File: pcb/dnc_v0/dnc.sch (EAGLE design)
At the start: 59 parts, among them IC1 74HC595D, IC2 74HC595D, Q1 200mA/50V, Q2 TSM2306CX, Q3 TSM2306CX, Q4 TSM2306CX, Q6 200mA/50V

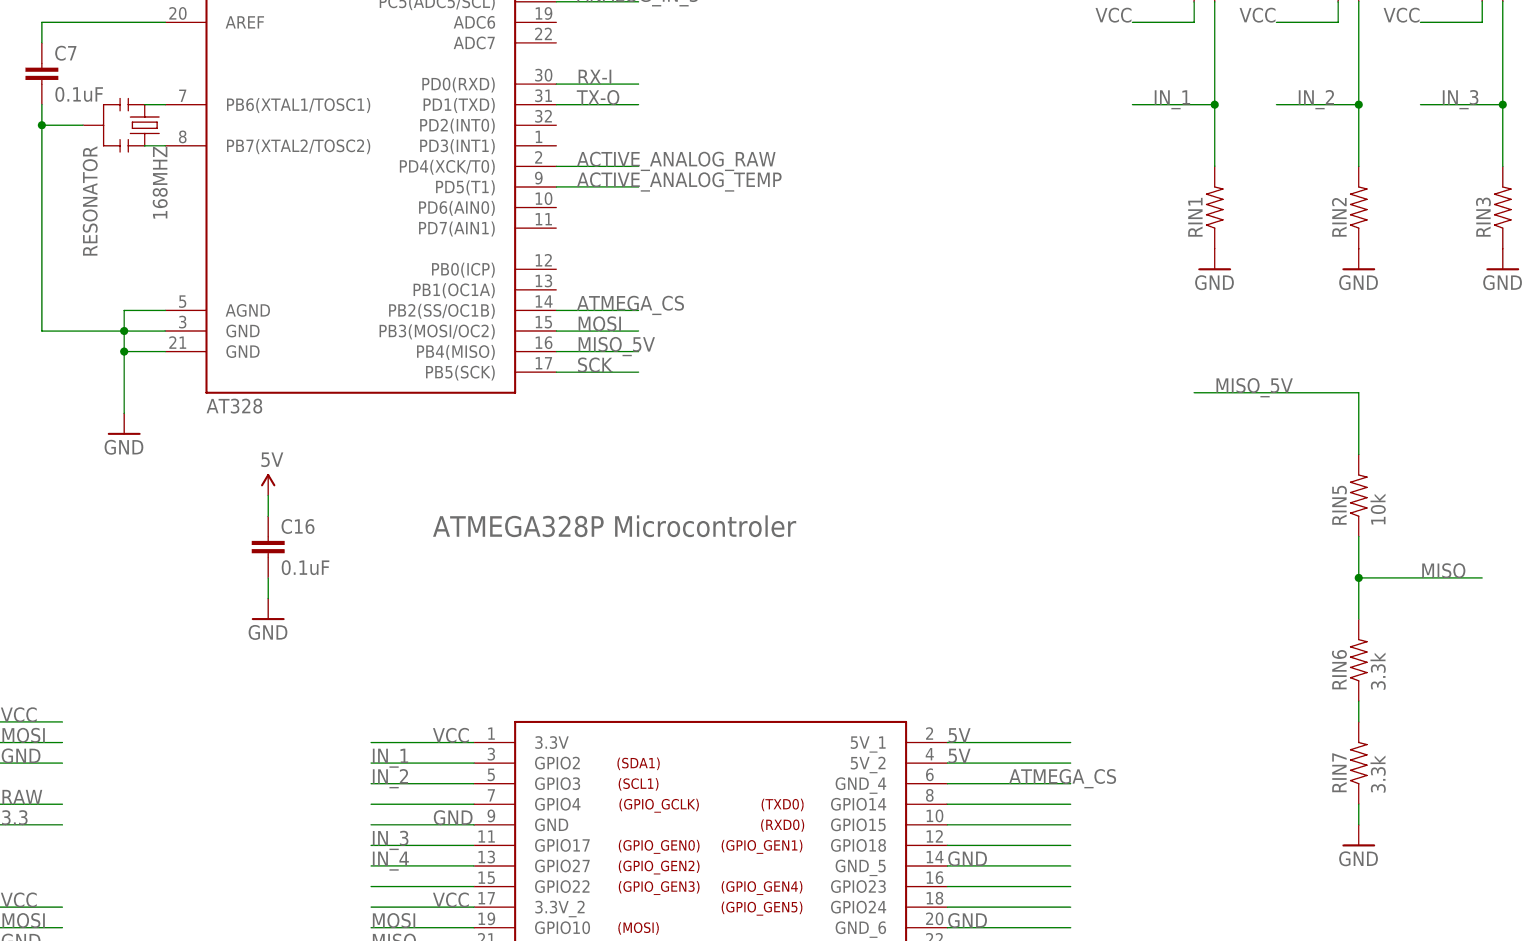
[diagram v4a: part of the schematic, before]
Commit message: Reorganize ATmega to work with 5V with Zener diode
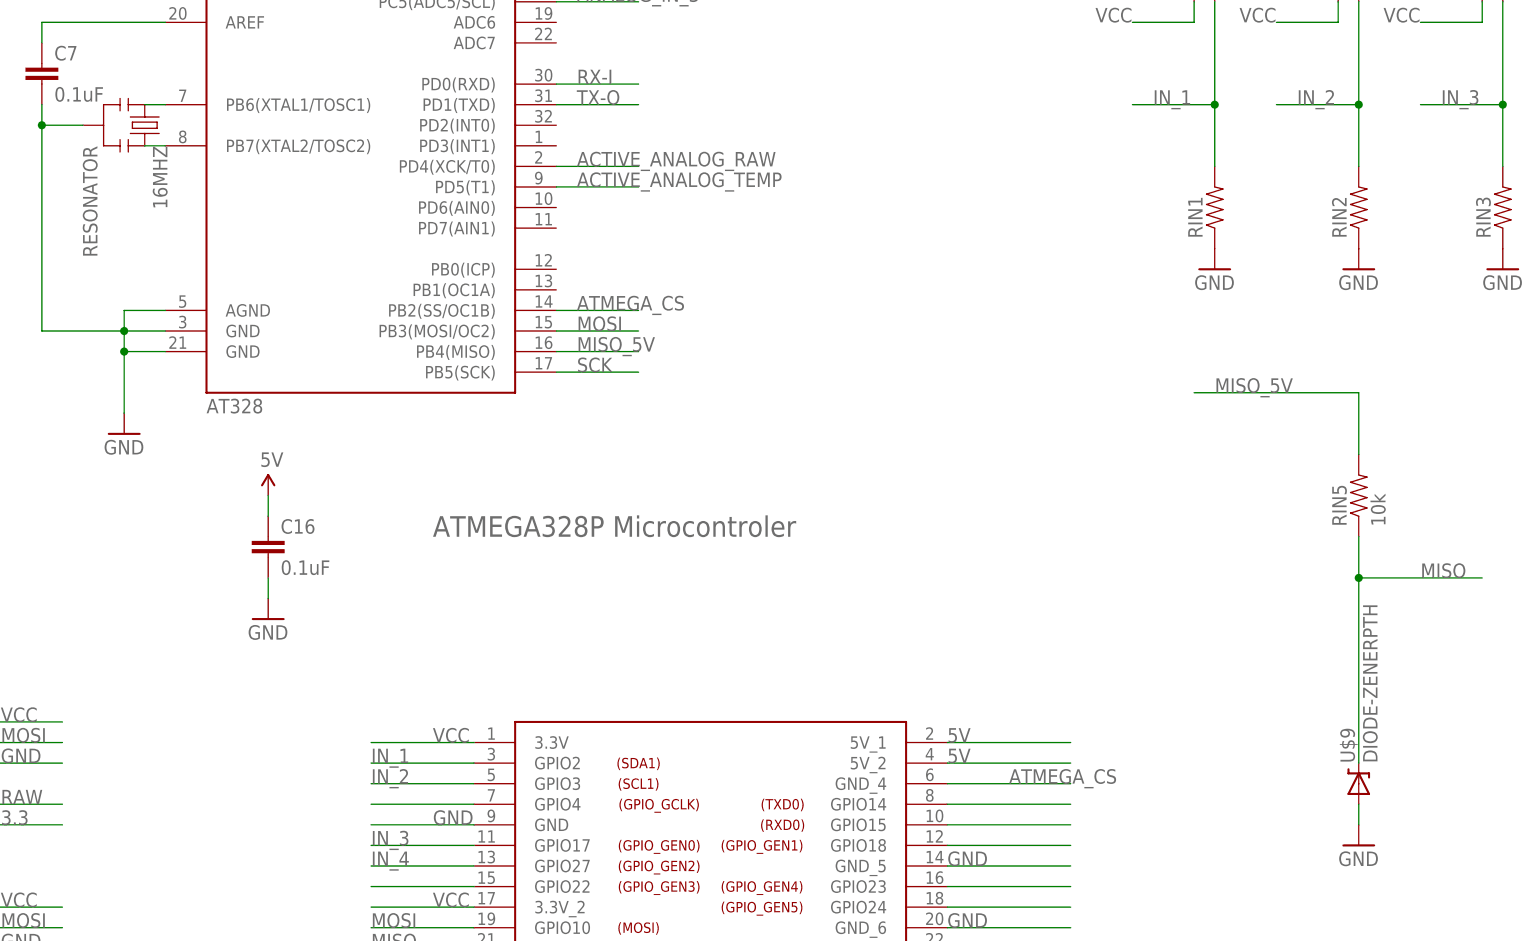
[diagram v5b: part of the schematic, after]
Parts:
- removed RIN6, RIN7: 3.3k, SparkFun-Passives:RESISTOR0603-RES
- added U$9: DIODE-ZENERPTH, SparkFun-DiscreteSemi:DIODE-ZENERPTH
- renumbered 168MHZ to 16MHZ
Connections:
- removed net N$6: RIN6.1, RIN7.2
- net GND: now also U$9.A; no longer RIN7.1
- net MISO: now also U$9.C; no longer RIN6.2
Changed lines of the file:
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@@
 <part name="GND36" library="SparkFun" deviceset="GND" device=""/>
 <part name="AT328" library="SparkFun" deviceset="ATMEGA168" device=""/>
-<part name="168MHZ" library="pierre_vv" deviceset="RESONATOR" device=""/>
+<part name="16MHZ" library="pierre_vv" deviceset="RESONATOR" device=""/>
 <part name="U$17" library="SparkFun" deviceset="5V" device="" value="5V"/>
 <part name="U$18" library="SparkFun" deviceset="5V" device=""/>
@@
 <part name="JP1" library="SparkFun-Connectors" deviceset="M02" device="5MM" value="M025MM"/>
 <part name="RIN5" library="SparkFun-Passives" deviceset="RESISTOR" device="0603-RES" value="10k"/>
-<part name="RIN6" library="SparkFun-Passives" deviceset="RESISTOR" device="0603-RES" value="3.3k"/>
-<part name="RIN7" library="SparkFun-Passives" deviceset="RESISTOR" device="0603-RES" value="3.3k"/>
 <part name="GND2" library="SparkFun-Aesthetics" deviceset="GND" device=""/>
+<part name="U$9" library="SparkFun-DiscreteSemi" deviceset="DIODE-ZENER" device="PTH"/>
 </parts>
 <sheets>
@@
 <instance part="GND36" gate="1" x="33.02" y="15.24"/>
 <instance part="AT328" gate="G$1" x="43.18" y="78.74"/>
-<instance part="168MHZ" gate="G$1" x="15.24" y="76.2" rot="R270"/>
+<instance part="16MHZ" gate="G$1" x="15.24" y="76.2" rot="R270"/>
 <instance part="U$17" gate="G$1" x="5.08" y="109.22"/>
 <instance part="U$18" gate="G$1" x="-38.1" y="99.06"/>
@@
 <instance part="JP1" gate="G$1" x="-160.02" y="96.52" rot="MR180"/>
 <instance part="RIN5" gate="G$1" x="167.64" y="30.48" rot="R90"/>
-<instance part="RIN6" gate="G$1" x="167.64" y="10.16" rot="R90"/>
-<instance part="RIN7" gate="G$1" x="167.64" y="-2.54" rot="R90"/>
 <instance part="GND2" gate="1" x="167.64" y="-12.7"/>
+<instance part="U$9" gate="G$1" x="167.64" y="-5.08" rot="R90"/>
 </instances>
 <busses>
@@
 <pinref part="AT328" gate="G$1" pin="GND@2"/>
 <pinref part="AT328" gate="G$1" pin="AGND"/>
-<pinref part="168MHZ" gate="G$1" pin="2"/>
+<pinref part="16MHZ" gate="G$1" pin="2"/>
 </segment>
 <segment>
@@
 </segment>
 <segment>
-<pinref part="RIN7" gate="G$1" pin="1"/>
 <pinref part="GND2" gate="1" pin="GND"/>
 <wire x1="167.64" y1="-7.62" x2="167.64" y2="-10.16" width="0.1524" layer="91"/>
+<pinref part="U$9" gate="G$1" pin="A"/>
 </segment>
 </net>
@@
 <segment>
 <pinref part="RIN5" gate="G$1" pin="1"/>
-<pinref part="RIN6" gate="G$1" pin="2"/>
 <wire x1="167.64" y1="25.4" x2="167.64" y2="20.32" width="0.1524" layer="91"/>
-<wire x1="167.64" y1="20.32" x2="167.64" y2="15.24" width="0.1524" layer="91"/>
 <wire x1="167.64" y1="20.32" x2="182.88" y2="20.32" width="0.1524" layer="91"/>
 <junction x="167.64" y="20.32"/>
 <label x="175.26" y="20.32" size="1.778" layer="95"/>
+<pinref part="U$9" gate="G$1" pin="C"/>
+<wire x1="167.64" y1="20.32" x2="167.64" y2="-2.54" width="0.1524" layer="91"/>
 </segment>
 </net>
@@
 <segment>
 <wire x1="17.78" y1="78.74" x2="20.32" y2="78.74" width="0.1524" layer="91"/>
-<pinref part="168MHZ" gate="G$1" pin="1"/>
+<pinref part="16MHZ" gate="G$1" pin="1"/>
 <pinref part="AT328" gate="G$1" pin="PB6(XTAL1/TOSC1)"/>
 </segment>
@@
 <segment>
 <wire x1="17.78" y1="73.66" x2="20.32" y2="73.66" width="0.1524" layer="91"/>
-<pinref part="168MHZ" gate="G$1" pin="3"/>
+<pinref part="16MHZ" gate="G$1" pin="3"/>
 <pinref part="AT328" gate="G$1" pin="PB7(XTAL2/TOSC2)"/>
 </segment>
@@
 </segment>
 </net>
-<net name="N$6" class="0">
-<segment>
-<pinref part="RIN6" gate="G$1" pin="1"/>
-<pinref part="RIN7" gate="G$1" pin="2"/>
-<wire x1="167.64" y1="5.08" x2="167.64" y2="2.54" width="0.1524" layer="91"/>
-</segment>
-</net>

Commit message: Reorganize ATmega to work with 3.3V
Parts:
- removed RIN5: 10k, SparkFun-Passives:RESISTOR0603-RES
- removed U$9: DIODE-ZENERPTH, SparkFun-DiscreteSemi:DIODE-ZENERPTH
- added JP12, JP20, JP21: M02LOCK_LONGPADS, SparkFun-Connectors:M02LOCK_LONGPADS
- added R10, R11, R9: 10k, SparkFun-Passives:RESISTOR0603-RES
- R5, R6, R7: value (none) -> 100k
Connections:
- removed net MISO_5V: RIN5.2
- new net N$1: JP12.1, R9.2
- new net N$13: JP21.1, R11.2
- new net N$6: JP20.1, R10.2
- net 5V: no longer AT328.AVCC, AT328.VCC@1, AT328.VCC@2
- net ACTIVE_OUT_POWER_2: now also AT328.PD3(INT1)
- net ACTIVE_OUT_POWER_3: now also AT328.PD6(AIN0)
- net GND: now also JP12.2, JP20.2, JP21.2, R10.1, R11.1, R9.1; no longer U$9.A
- net MISO: no longer RIN5.1, U$9.C
- net VCC: now also AT328.AVCC, AT328.VCC@1, AT328.VCC@2

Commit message: Reogranise with 3.3, 5 and RAW
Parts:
- removed R10, R11, R9: 10k, SparkFun-Passives:RESISTOR0603-RES
- removed R5, R6, R7: 100k, SparkFun-Passives:RESISTOR0603-RES
- added JP22: (no value), SparkFun:M02PTH3
- added Q5, Q7, Q8: TSM2306CX, SparkFun-DiscreteSemi:MOSFET-NCHANNEL2N7002PW
- added RIN10, RIN5, RIN6, RIN7, RIN8, RIN9: 100k, SparkFun-Passives:RESISTOR0603-RES
- renumbered 16MHZ to 8MHZ
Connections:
- removed net 5V: C16.1, ISP1.2, JP2.2, JP3.2, JP4.2, PROG1.VCC, R26.2, R3.1, U$4.5V_1, U$4.5V_2, U$5.OUT+
- removed net N$1: JP12.1, R9.2
- removed net N$13: JP21.1, R11.2
- removed net N$26: R6.2
- removed net N$27: U$4.GPIO19
- removed net N$28: U$4.GPIO26
- removed net N$29: Q4.S, R7.2
- removed net N$40: U$4.GPIO12
- removed net N$6: JP20.1, R10.2
- new net +3V3: AT328.AVCC, AT328.VCC@1, AT328.VCC@2, C16.1, IC1A.SCL, IC2A.SCL, ISP1.2, JP2.2, JP22.1, JP3.2, JP4.2, JP5.1, JP6.1, JP7.1, JP8.1, PROG1.VCC, R26.2, U$4.3.3V, U$4.3.3V_2
- new net +5V: JP22.2, Q2.D, Q3.D, Q4.D, Q5.D, Q7.D, Q8.D, R3.1, U$4.5V_1, U$4.5V_2, U$5.OUT+
- new net ACTIVE_OUT_1: Q5.G, RIN8.2, U$4.GPIO12
- new net ACTIVE_OUT_2: Q7.G, RIN9.2, U$4.GPIO19
- new net ACTIVE_OUT_3: Q8.G, RIN10.2, U$4.GPIO26
- new net OUT_1: JP12.1, Q5.S
- new net OUT_2: JP20.1, Q7.S
- new net OUT_3: JP21.1, Q8.S
- net ACTIVE_OUT_POWER_1: now also RIN5.2
- net ACTIVE_OUT_POWER_2: now also RIN6.2
- net ACTIVE_OUT_POWER_3: now also RIN7.2
- net GND: now also IC1A.G, IC2A.G, RIN10.1, RIN5.1, RIN6.1, RIN7.1, RIN8.1, RIN9.1; no longer R10.1, R11.1, R5.1, R6.1, R7.1, R9.1
- net OUT_POWER_2: no longer R5.2
- net OUT_POWER_3: now also Q4.S
- net RAW: no longer Q2.D, Q3.D, Q4.D
- net VCC: no longer AT328.AVCC, AT328.VCC@1, AT328.VCC@2, JP5.1, JP6.1, JP7.1, JP8.1, U$4.3.3V, U$4.3.3V_2
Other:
- moved on the sheet: JP20, JP21

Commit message: Some little corrections
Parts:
- added R5: 100k, SparkFun-Passives:RESISTOR0603-RES
- R1: value (none) -> 100k
- R2: value (none) -> 10k
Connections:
- net ACTIVE_ANALOG_TEMP: now also R5.1
- net GND: now also R5.2
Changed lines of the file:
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@@
 <part name="U$4" library="pierre_vv" deviceset="RASPIA+" device=""/>
 <part name="U$5" library="pierre_vv" deviceset="DC/DC_SEED" device=""/>
-<part name="R1" library="SparkFun-Passives" deviceset="RESISTOR" device="0603-RES"/>
-<part name="R2" library="SparkFun-Passives" deviceset="RESISTOR" device="0603-RES"/>
+<part name="R1" library="SparkFun-Passives" deviceset="RESISTOR" device="0603-RES" value="100k"/>
+<part name="R2" library="SparkFun-Passives" deviceset="RESISTOR" device="0603-RES" value="10k"/>
 <part name="GND6" library="SparkFun-Aesthetics" deviceset="GND" device=""/>
 <part name="IC2" library="74xx-eu" deviceset="74*595" device="D" technology="HC"/>
@@
 <part name="GND7" library="SparkFun-Aesthetics" deviceset="GND" device=""/>
 <part name="GND8" library="SparkFun" deviceset="GND" device=""/>
-<part name="P+6" library="supply1" deviceset="+5V" device=""/>
-<part name="+3V1" library="supply1" deviceset="+3V3" device=""/>
-<part name="U$9" library="pierre_vv" deviceset="RAW" device=""/>
-<part name="P+7" library="supply1" deviceset="+5V" device=""/>
-<part name="+3V2" library="supply1" deviceset="+3V3" device=""/>
-<part name="U$10" library="pierre_vv" deviceset="RAW" device=""/>
 <part name="JP22" library="SparkFun" deviceset="M02" device="PTH3"/>
 <part name="P+1" library="supply1" deviceset="+5V" device=""/>
@@
 <part name="P+8" library="supply1" deviceset="+5V" device=""/>
 <part name="GND29" library="SparkFun-Aesthetics" deviceset="GND" device=""/>
+<part name="R5" library="SparkFun-Passives" deviceset="RESISTOR" device="0603-RES" value="100k"/>
+<part name="GND30" library="SparkFun-Aesthetics" deviceset="GND" device=""/>
 </parts>
 <sheets>
@@
 <instance part="GND7" gate="1" x="335.28" y="78.74"/>
 <instance part="GND8" gate="1" x="-172.72" y="-68.58"/>
-<instance part="P+6" gate="1" x="-43.18" y="50.8"/>
-<instance part="+3V1" gate="G$1" x="-35.56" y="50.8"/>
-<instance part="U$9" gate="G$1" x="-27.94" y="48.26"/>
-<instance part="P+7" gate="1" x="-43.18" y="40.64"/>
-<instance part="+3V2" gate="G$1" x="-35.56" y="40.64"/>
-<instance part="U$10" gate="G$1" x="-27.94" y="38.1"/>
 <instance part="JP22" gate="G$1" x="-15.24" y="91.44" rot="R90"/>
 <instance part="P+1" gate="1" x="-38.1" y="101.6"/>
@@
 <instance part="P+8" gate="1" x="276.86" y="-30.48"/>
 <instance part="GND29" gate="1" x="254" y="-83.82"/>
+<instance part="R5" gate="G$1" x="-60.96" y="137.16" rot="R90"/>
+<instance part="GND30" gate="1" x="-60.96" y="149.86" rot="R180"/>
 </instances>
 <busses>
@@
 <wire x1="254" y1="-81.28" x2="254" y2="-71.12" width="0.1524" layer="91"/>
 </segment>
+<segment>
+<pinref part="R5" gate="G$1" pin="2"/>
+<pinref part="GND30" gate="1" pin="GND"/>
+<wire x1="-60.96" y1="142.24" x2="-60.96" y2="147.32" width="0.1524" layer="91"/>
+</segment>
 </net>
 <net name="VCC" class="0">
@@
 <net name="ACTIVE_ANALOG_TEMP" class="0">
 <segment>
-<wire x1="-53.34" y1="119.38" x2="-68.58" y2="119.38" width="0.1524" layer="91"/>
+<wire x1="-53.34" y1="119.38" x2="-60.96" y2="119.38" width="0.1524" layer="91"/>
 <label x="-81.28" y="119.38" size="1.778" layer="95"/>
 <pinref part="Q6" gate="G$1" pin="G"/>
-</segment>
-</net>
+<pinref part="R5" gate="G$1" pin="1"/>
+<wire x1="-60.96" y1="119.38" x2="-68.58" y2="119.38" width="0.1524" layer="91"/>
+<wire x1="-60.96" y1="132.08" x2="-60.96" y2="119.38" width="0.1524" layer="91"/>
+<junction x="-60.96" y="119.38"/>
+</segment>
+</net>
